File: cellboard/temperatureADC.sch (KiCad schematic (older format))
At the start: 15 parts, among them J16 Conn_02x06_Top_Bottom, U20 MCP1811AT-033LT, U6 ADC128D818

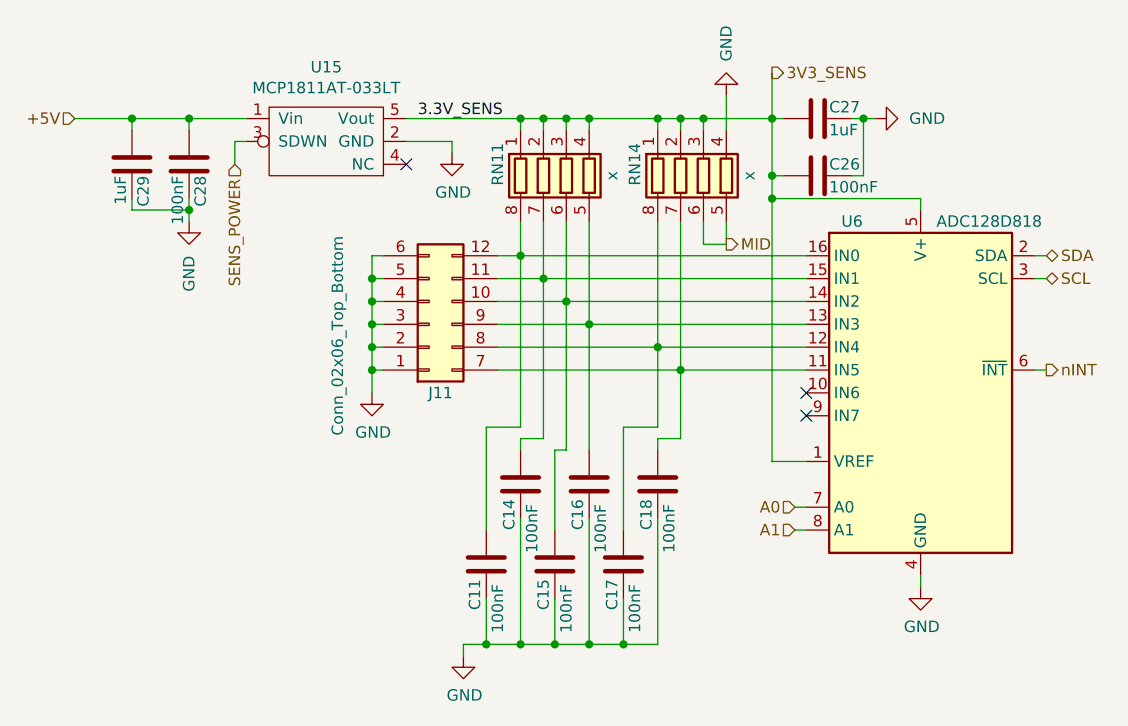
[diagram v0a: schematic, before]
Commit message: changed footprint mcp1811
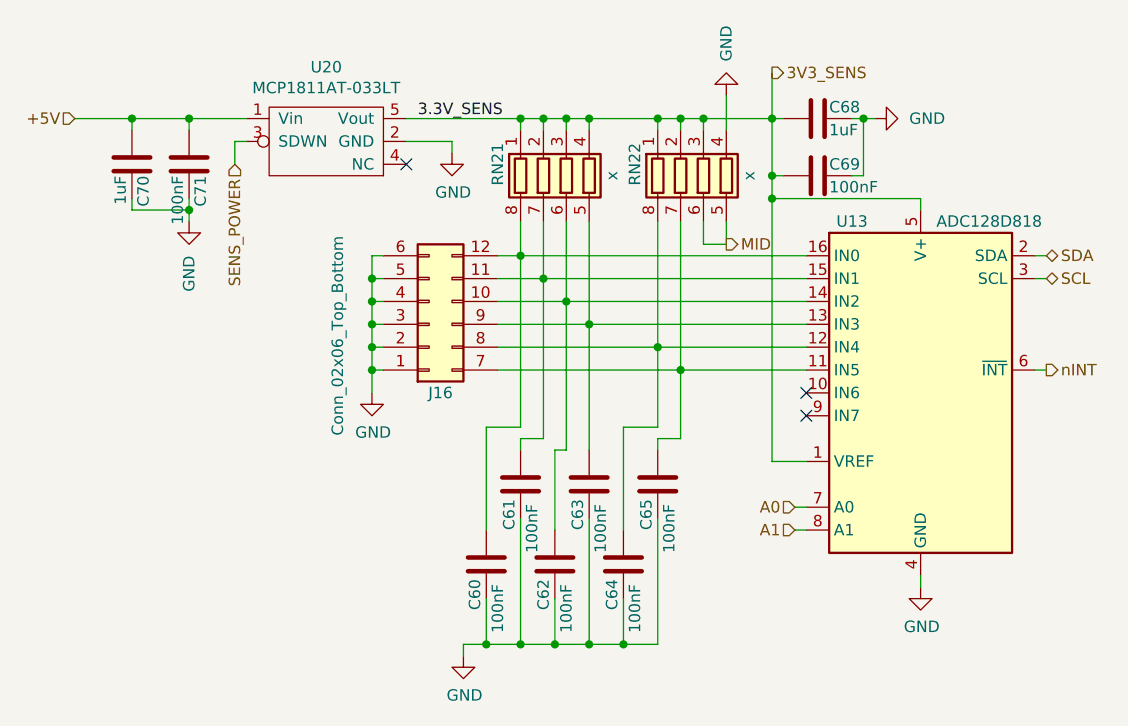
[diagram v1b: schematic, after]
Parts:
- U20: footprint Package_TO_SOT_SMD:SOT-23-5_HandSoldering -> Package_TO_SOT_SMD:SOT-353_SC-70-5
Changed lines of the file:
@@
 $Descr A4 11693 8268
 encoding utf-8
-Sheet 6 11
+Sheet 11 11
 Title "Fenice BMS - CellBoard"
 Date "2021-06-11"
@@
 AR Path="/60CD4EA2/60E7E963/604F734D" Ref="U9"  Part="1"
 AR Path="/60CD4EA2/603CB94B/604F734D" Ref="U13"  Part="1"
-F 0 "U6" H 5200 3900 50  0000 C CNN
+F 0 "U13" H 5200 3900 50  0000 C CNN
 F 1 "ADC128D818" H 5800 3900 50  0000 C CNN
 F 2 "CellsBoard:TSSOP-16_4.4x5mm_P0.65mm" H 5500 3150 50  0001 C CIN
@@
 AR Path="/60CD4EA2/60E7E963/604FB178" Ref="#PWR085"  Part="1"
 AR Path="/60CD4EA2/603CB94B/604FB178" Ref="#PWR092"  Part="1"
-F 0 "#PWR071" H 5500 3750 50  0001 C CNN
+F 0 "#PWR092" H 5500 3750 50  0001 C CNN
 F 1 "GND" H 5505 3827 50  0000 C CNN
 F 2 "" H 5500 4000 50  0001 C CNN
@@
 AR Path="/60CD4EA2/60E7E963/60530696" Ref="RN15"  Part="1"
 AR Path="/60CD4EA2/603CB94B/60530696" Ref="RN21"  Part="1"
-F 0 "RN11" V 3650 2150 50  0000 C CNN
+F 0 "RN21" V 3650 2150 50  0000 C CNN
 F 1 "x" V 4150 2200 50  0000 C CNN
 F 2 "Resistor_SMD:R_Array_Convex_4x0603" V 4225 2200 50  0001 C CNN
@@
 AR Path="/60CD4EA2/60E7E963/605310D0" Ref="RN16"  Part="1"
 AR Path="/60CD4EA2/603CB94B/605310D0" Ref="RN22"  Part="1"
-F 0 "RN14" V 4250 2150 50  0000 C CNN
+F 0 "RN22" V 4250 2150 50  0000 C CNN
 F 1 "x" V 4750 2200 50  0000 C CNN
 F 2 "Resistor_SMD:R_Array_Convex_4x0603" V 4825 2200 50  0001 C CNN
@@
 AR Path="/60CD4EA2/60E7E963/6054A4BC" Ref="C41"  Part="1"
 AR Path="/60CD4EA2/603CB94B/6054A4BC" Ref="C65"  Part="1"
-F 0 "C18" V 4300 3350 50  0000 L CNN
+F 0 "C65" V 4300 3350 50  0000 L CNN
 F 1 "100nF" V 4400 3250 50  0000 L CNN
 F 2 "Capacitor_SMD:C_0603_1608Metric" H 4388 3400 50  0001 C CNN
@@
 AR Path="/60CD4EA2/60E7E963/605584AB" Ref="C40"  Part="1"
 AR Path="/60CD4EA2/603CB94B/605584AB" Ref="C64"  Part="1"
-F 0 "C17" V 4150 3700 50  0000 L CNN
+F 0 "C64" V 4150 3700 50  0000 L CNN
 F 1 "100nF" V 4250 3600 50  0000 L CNN
 F 2 "Capacitor_SMD:C_0603_1608Metric" H 4238 3750 50  0001 C CNN
@@
 AR Path="/60CD4EA2/60E7E963/605587FC" Ref="C39"  Part="1"
 AR Path="/60CD4EA2/603CB94B/605587FC" Ref="C63"  Part="1"
-F 0 "C16" V 4000 3350 50  0000 L CNN
+F 0 "C63" V 4000 3350 50  0000 L CNN
 F 1 "100nF" V 4100 3250 50  0000 L CNN
 F 2 "Capacitor_SMD:C_0603_1608Metric" H 4088 3400 50  0001 C CNN
@@
 AR Path="/60CD4EA2/60E7E963/6056673B" Ref="C36"  Part="1"
 AR Path="/60CD4EA2/603CB94B/6056673B" Ref="C60"  Part="1"
-F 0 "C11" V 3550 3700 50  0000 L CNN
+F 0 "C60" V 3550 3700 50  0000 L CNN
 F 1 "100nF" V 3650 3600 50  0000 L CNN
 F 2 "Capacitor_SMD:C_0603_1608Metric" H 3638 3750 50  0001 C CNN
@@
 AR Path="/60CD4EA2/60E7E963/60566AAA" Ref="C38"  Part="1"
 AR Path="/60CD4EA2/603CB94B/60566AAA" Ref="C62"  Part="1"
-F 0 "C15" V 3850 3700 50  0000 L CNN
+F 0 "C62" V 3850 3700 50  0000 L CNN
 F 1 "100nF" V 3950 3600 50  0000 L CNN
 F 2 "Capacitor_SMD:C_0603_1608Metric" H 3938 3750 50  0001 C CNN
@@
 AR Path="/60CD4EA2/60E7E963/605671D5" Ref="C37"  Part="1"
 AR Path="/60CD4EA2/603CB94B/605671D5" Ref="C61"  Part="1"
-F 0 "C14" V 3700 3350 50  0000 L CNN
+F 0 "C61" V 3700 3350 50  0000 L CNN
 F 1 "100nF" V 3800 3250 50  0000 L CNN
 F 2 "Capacitor_SMD:C_0603_1608Metric" H 3788 3400 50  0001 C CNN
@@
 AR Path="/60CD4EA2/60E7E963/6059FDFF" Ref="#PWR082"  Part="1"
 AR Path="/60CD4EA2/603CB94B/6059FDFF" Ref="#PWR089"  Part="1"
-F 0 "#PWR068" H 3500 4050 50  0001 C CNN
+F 0 "#PWR089" H 3500 4050 50  0001 C CNN
 F 1 "GND" H 3505 4127 50  0000 C CNN
 F 2 "" H 3500 4300 50  0001 C CNN
@@
 AR Path="/60CD4EA2/60E7E963/605CF54A" Ref="C42"  Part="1"
 AR Path="/60CD4EA2/603CB94B/605CF54A" Ref="C69"  Part="1"
-F 0 "C26" V 5000 2250 50  0000 L CNN
+F 0 "C69" V 5000 2250 50  0000 L CNN
 F 1 "100nF" V 5100 2250 50  0000 L CNN
 F 2 "Capacitor_SMD:C_0603_1608Metric" H 5088 2050 50  0001 C CNN
@@
 AR Path="/60CD4EA2/60E7E963/605D8DEB" Ref="#PWR079"  Part="1"
 AR Path="/60CD4EA2/603CB94B/605D8DEB" Ref="#PWR086"  Part="1"
-F 0 "#PWR065" H 2300 2150 50  0001 C CNN
+F 0 "#PWR086" H 2300 2150 50  0001 C CNN
 F 1 "GND" V 2300 2250 50  0000 R CNN
 F 2 "" H 2300 2400 50  0001 C CNN
@@
 AR Path="/60CD4EA2/60E7E963/605CD7AA" Ref="C43"  Part="1"
 AR Path="/60CD4EA2/603CB94B/605CD7AA" Ref="C68"  Part="1"
-F 0 "C27" V 5000 2000 50  0000 L CNN
+F 0 "C68" V 5000 2000 50  0000 L CNN
 F 1 "1uF" V 5100 2000 50  0000 L CNN
 F 2 "Capacitor_SMD:C_0603_1608Metric" H 5088 1800 50  0001 C CNN
@@
 AR Path="/60CD4EA2/60E7E963/6033FEB4" Ref="C54"  Part="1"
 AR Path="/60CD4EA2/603CB94B/6033FEB4" Ref="C71"  Part="1"
-F 0 "C28" V 2250 2200 50  0000 L CNN
+F 0 "C71" V 2250 2200 50  0000 L CNN
 F 1 "100nF" V 2350 2200 50  0000 L CNN
 F 2 "Capacitor_SMD:C_0603_1608Metric" H 2338 2000 50  0001 C CNN
@@
 AR Path="/60CD4EA2/60E7E963/603403C8" Ref="C55"  Part="1"
 AR Path="/60CD4EA2/603CB94B/603403C8" Ref="C70"  Part="1"
-F 0 "C29" V 2000 2200 50  0000 L CNN
+F 0 "C70" V 2000 2200 50  0000 L CNN
 F 1 "1uF" V 2100 2200 50  0000 L CNN
 F 2 "Capacitor_SMD:C_0603_1608Metric" H 2088 2000 50  0001 C CNN
@@
 AR Path="/60CD4EA2/60E7E963/60354C60" Ref="#PWR084"  Part="1"
 AR Path="/60CD4EA2/603CB94B/60354C60" Ref="#PWR091"  Part="1"
-F 0 "#PWR070" H 5300 1700 50  0001 C CNN
+F 0 "#PWR091" H 5300 1700 50  0001 C CNN
 F 1 "GND" V 5300 1800 50  0000 R CNN
 F 2 "" H 5300 1950 50  0001 C CNN
@@
 AR Path="/60CD4EA2/60E7E963/605C003B" Ref="#PWR081"  Part="1"
 AR Path="/60CD4EA2/603CB94B/605C003B" Ref="#PWR088"  Part="1"
-F 0 "#PWR067" H 3450 1850 50  0001 C CNN
+F 0 "#PWR088" H 3450 1850 50  0001 C CNN
 F 1 "GND" H 3455 1927 50  0000 C CNN
 F 2 "" H 3450 2100 50  0001 C CNN
@@
 AR Path="/60CD4EA2/60E7E963/60B91754" Ref="J15"  Part="1"
 AR Path="/60CD4EA2/603CB94B/60B91754" Ref="J16"  Part="1"
-F 0 "J11" H 3400 3150 50  0000 C CNN
+F 0 "J16" H 3400 3150 50  0000 C CNN
 F 1 "Conn_02x06_Top_Bottom" V 2950 2900 50  0000 C CNN
 F 2 "Connector_Molex:Molex_Nano-Fit_105310-xx12_2x06_P2.50mm_Vertical" H 3350 2850 50  0001 C CNN
@@
 AR Path="/60CD4EA2/60E7E963/60ECE2A8" Ref="#PWR080"  Part="1"
 AR Path="/60CD4EA2/603CB94B/60ECE2A8" Ref="#PWR087"  Part="1"
-F 0 "#PWR066" H 3100 2900 50  0001 C CNN
+F 0 "#PWR087" H 3100 2900 50  0001 C CNN
 F 1 "GND" H 3105 2977 50  0000 C CNN
 F 2 "" H 3100 3150 50  0001 C CNN
@@
 AR Path="/60CD4EA2/60E7E963/6112B493" Ref="#PWR083"  Part="1"
 AR Path="/60CD4EA2/603CB94B/6112B493" Ref="#PWR090"  Part="1"
-F 0 "#PWR069" H 4650 1600 50  0001 C CNN
+F 0 "#PWR090" H 4650 1600 50  0001 C CNN
 F 1 "GND" V 4650 1700 50  0000 R CNN
 F 2 "" H 4650 1850 50  0001 C CNN
@@
 AR Path="/60CD4EA2/60E7E963/60BCF9F8" Ref="U19"  Part="1"
 AR Path="/60CD4EA2/603CB94B/60BCF9F8" Ref="U20"  Part="1"
-F 0 "U15" H 2900 2375 50  0000 C CNN
+F 0 "U20" H 2900 2375 50  0000 C CNN
 F 1 "MCP1811AT-033LT" H 2900 2284 50  0000 C CNN
-F 2 "Package_TO_SOT_SMD:SOT-23-5_HandSoldering" H 2600 2200 50  0001 C CNN
+F 2 "Package_TO_SOT_SMD:SOT-353_SC-70-5" H 2600 2200 50  0001 C CNN
 F 3 "" H 2600 2200 50  0001 C CNN
 	1    2900 2050
